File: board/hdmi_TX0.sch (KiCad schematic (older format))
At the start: 21 parts

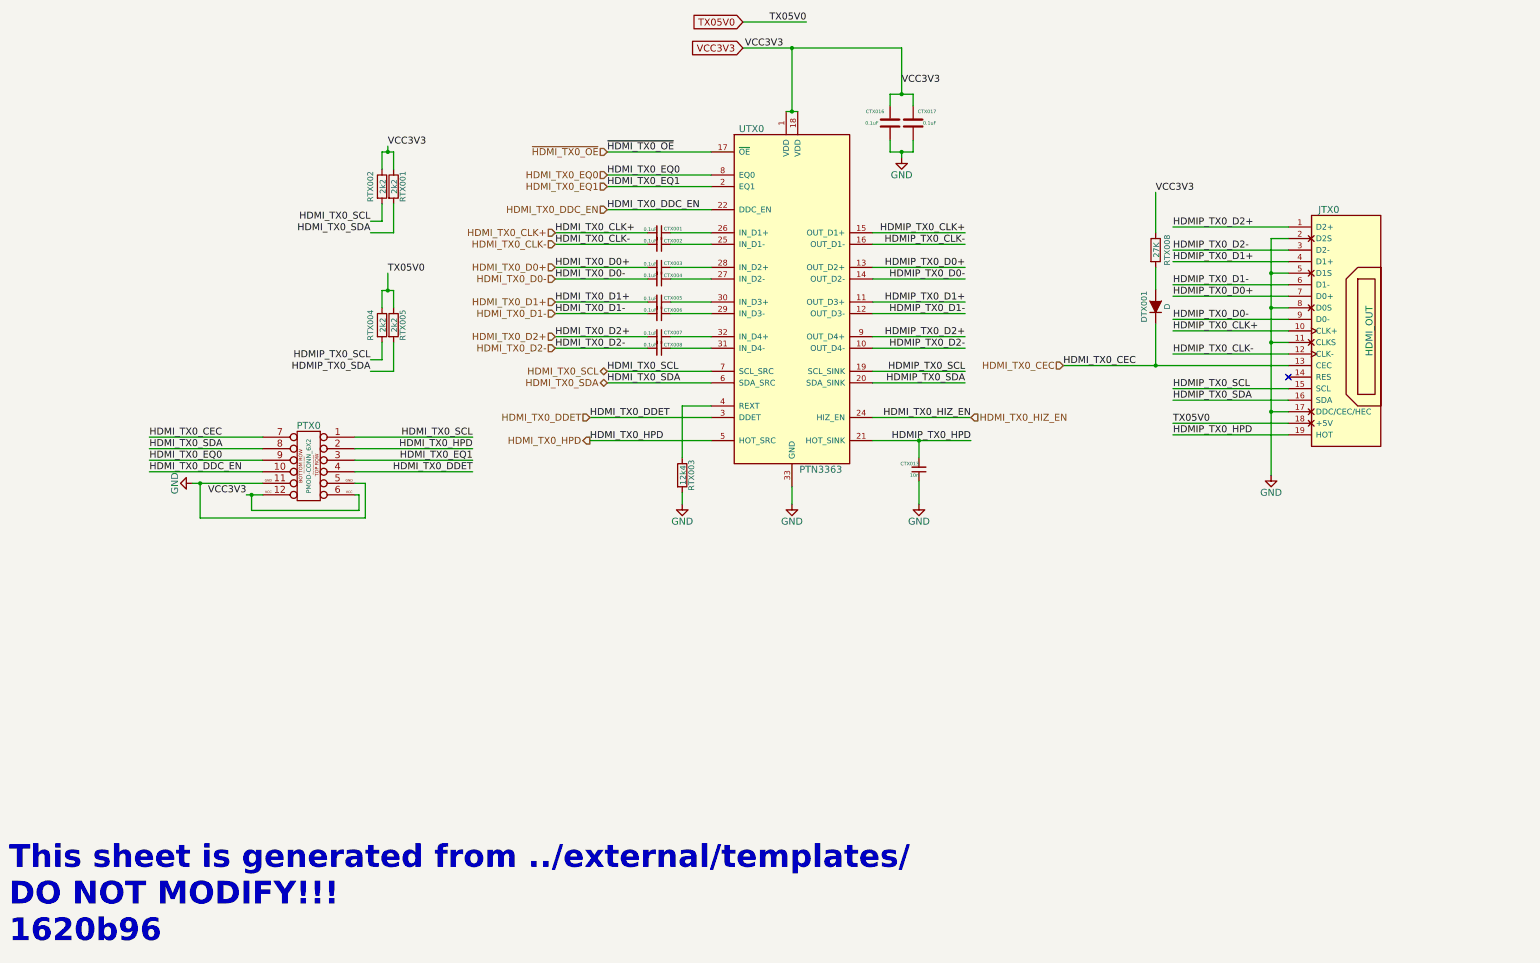
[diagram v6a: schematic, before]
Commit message: Update from template.
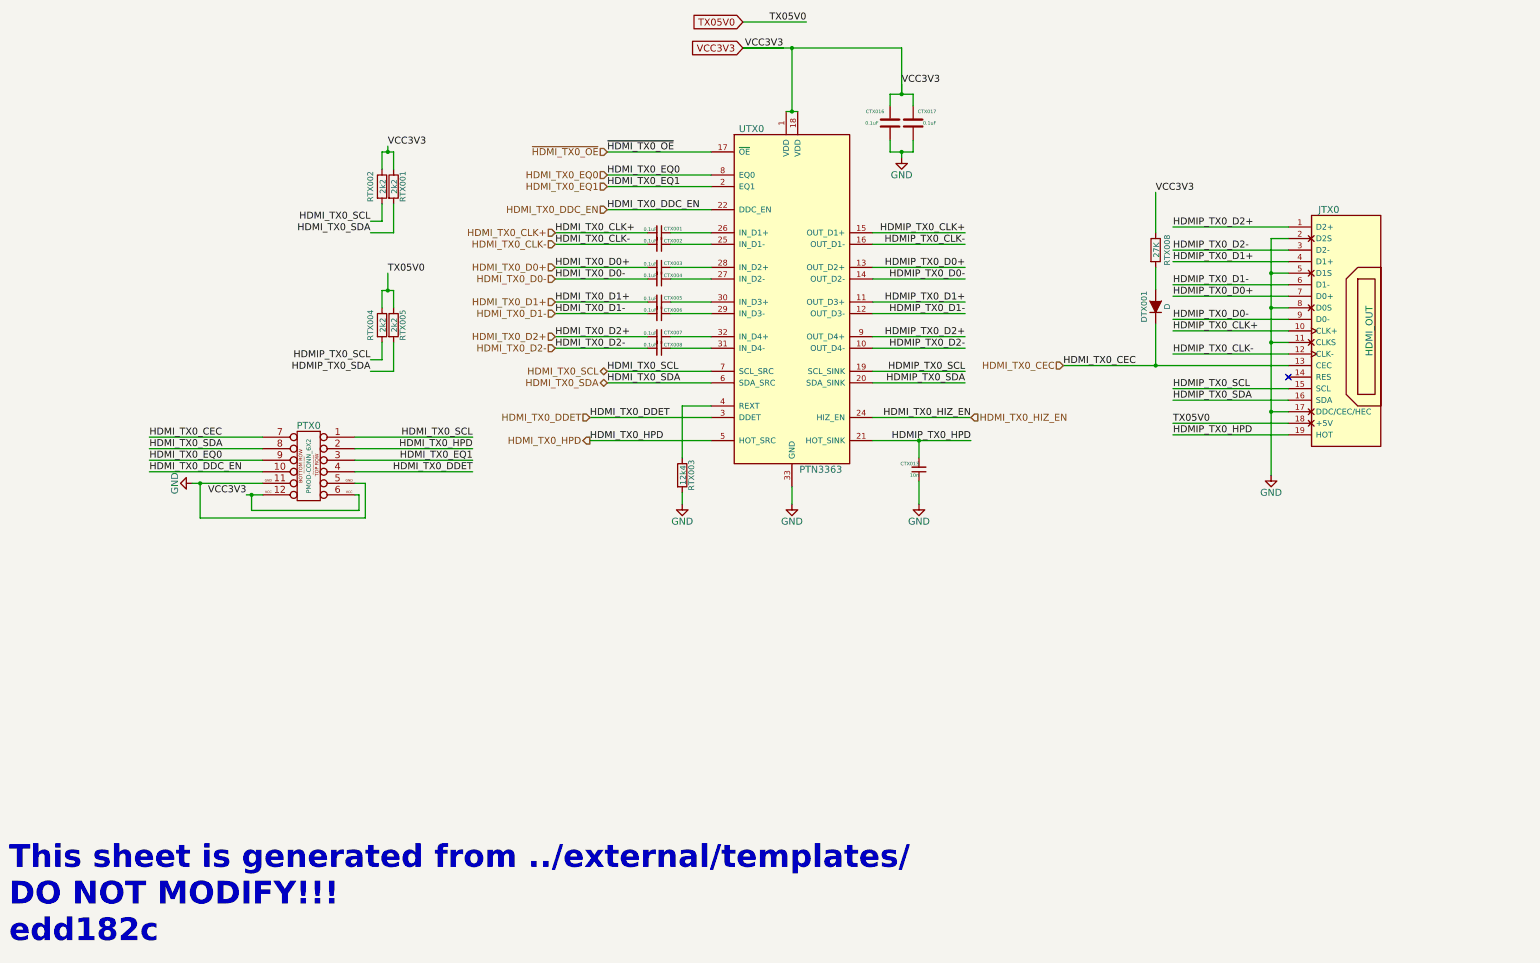
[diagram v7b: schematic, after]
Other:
- note added: "This sheet is generated from ../external/templates/\nDO NOT MODIFY!!!\nedd182c"
- note removed: "This sheet is generated from ../external/templates/\nDO NOT MODIFY!!!\n1620b96"
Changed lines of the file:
@@
 LIBS:contrib
 LIBS:valves
-LIBS:pmod
+LIBS:pmod-conn_6x2
+LIBS:ma78l00
 LIBS:hdmi
 LIBS:ptn3363
-LIBS:ma78l00
-LIBS:pmod-conn_6x2
-LIBS:EEPROM
-LIBS:xc9140
-LIBS:reg710-dbv
-LIBS:pmod-hdmi-tx-cache
 EELAYER 25 0
 EELAYER END
 $Descr A3 16535 11693
 encoding utf-8
-Sheet 2 2
+Sheet 1 1
 Title ""
 Date ""
@@
 HDMIP_TX0_HPD
 $Comp
-L GND #PWR010
+L GND #PWR106
 U 1 1 57B7C214
 P 7450 7150
-F 0 "#PWR010" H 7450 6900 60  0001 C CNN
+F 0 "#PWR106" H 7450 6900 60  0001 C CNN
 F 1 "GND" H 7450 7000 60  0000 C CNN
 F 2 "" H 7450 7150 60  0000 C CNN
@@
 $EndComp
 $Comp
-L GND #PWR011
+L GND #PWR112
 U 1 1 57C0774B
 P 11600 6900
-F 0 "#PWR011" H 11600 6650 60  0001 C CNN
+F 0 "#PWR112" H 11600 6650 60  0001 C CNN
 F 1 "GND" H 11600 6750 60  0000 C CNN
 F 2 "" H 11600 6900 60  0000 C CNN
@@
 AR Path="/57C07751" Ref="RTX008"  Part="1"
 AR Path="/57C01383/57C07751" Ref="RTX003"  Part="1"
-AR Path="/5802F547/57C07751" Ref="RTX008"  Part="1"
 F 0 "RTX008" V 10700 4950 50  0000 C CNN
 F 1 "27K" V 10607 4951 50  0000 C CNN
@@
 AR Path="/57C07753" Ref="RTX002"  Part="1"
 AR Path="/57C01383/57C07753" Ref="RTX001"  Part="1"
-AR Path="/5802F547/57C07753" Ref="RTX002"  Part="1"
 F 0 "RTX002" V 3800 4400 50  0000 C CNN
 F 1 "2k2" V 3907 4401 50  0000 C CNN
@@
 AR Path="/57C07755" Ref="RTX001"  Part="1"
 AR Path="/57C01383/57C07755" Ref="RTX002"  Part="1"
-AR Path="/5802F547/57C07755" Ref="RTX001"  Part="1"
 F 0 "RTX001" V 4080 4400 50  0000 C CNN
 F 1 "2k2" V 4007 4401 50  0000 C CNN
@@
 	11750 4850 11600 4850
 Wire Wire Line
-	11600 4850 11600 6900
+	11600 4850 11600 5150
+Wire Wire Line
+	11600 5150 11600 5450
+Wire Wire Line
+	11600 5450 11600 5750
+Wire Wire Line
+	11600 5750 11600 6350
+Wire Wire Line
+	11600 6350 11600 6900
 Wire Wire Line
 	11750 5150 11600 5150
@@
 	6400 5800 6750 5800
 Wire Wire Line
-	8150 6600 9000 6600
+	8150 6600 8550 6600
+Wire Wire Line
+	8550 6600 9000 6600
 Wire Wire Line
 	8150 6400 9000 6400
 Wire Wire Line
-	7400 3750 7500 3750
-Wire Wire Line
-	7450 3200 7450 3750
+	7400 3750 7450 3750
+Wire Wire Line
+	7450 3750 7500 3750
+Wire Wire Line
+	7450 3750 7450 3200
 Connection ~ 7450 3750
 Wire Wire Line
@@
 Connection ~ 11600 6350
 Wire Wire Line
-	9800 5950 11750 5950
+	9800 5950 10600 5950
+Wire Wire Line
+	10600 5950 11750 5950
 Wire Wire Line
 	10600 5950 10600 5590
@@
 	4000 4100 4000 4250
 Wire Wire Line
-	3900 4100 4000 4100
+	3900 4100 3950 4100
+Wire Wire Line
+	3950 4100 4000 4100
 Text Label 3800 5900 2    60   ~ 0
 HDMIP_TX0_SCL
@@
 AR Path="/57C07769" Ref="RTX004"  Part="1"
 AR Path="/57C01383/57C07769" Ref="RTX004"  Part="1"
-AR Path="/5802F547/57C07769" Ref="RTX004"  Part="1"
 F 0 "RTX004" V 3800 5600 50  0000 C CNN
 F 1 "2k2" V 3907 5601 50  0000 C CNN
@@
 AR Path="/57B7FCE7" Ref="RTX005"  Part="1"
 AR Path="/57C01383/57B7FCE7" Ref="RTX005"  Part="1"
-AR Path="/5802F547/57B7FCE7" Ref="RTX005"  Part="1"
 F 0 "RTX005" V 4080 5600 50  0000 C CNN
 F 1 "2k2" V 4007 5601 50  0000 C CNN
@@
 AR Path="/57C0776D" Ref="RTX003"  Part="1"
 AR Path="/57C01383/57C0776D" Ref="RTX006"  Part="1"
-AR Path="/5802F547/57C0776D" Ref="RTX003"  Part="1"
 F 0 "RTX003" V 6580 6900 50  0000 C CNN
 F 1 "12k4" V 6507 6901 50  0000 C CNN
@@
 	6500 6300 6500 6750
 $Comp
-L GND #PWR012
+L GND #PWR104
 U 1 1 57C0776F
 P 6500 7150
-F 0 "#PWR012" H 6500 6900 60  0001 C CNN
+F 0 "#PWR104" H 6500 6900 60  0001 C CNN
 F 1 "GND" H 6500 7000 60  0000 C CNN
 F 2 "" H 6500 7150 60  0000 C CNN
@@
 	3900 5300 3900 5450
 Wire Wire Line
-	3900 5300 4000 5300
+	3900 5300 3950 5300
+Wire Wire Line
+	3950 5300 4000 5300
 Wire Wire Line
 	4000 5300 4000 5450
@@
 $EndComp
 $Comp
-L GND #PWR013
+L GND #PWR109
 U 1 1 57C07776
 P 8550 7150
-F 0 "#PWR013" H 8550 6900 60  0001 C CNN
+F 0 "#PWR109" H 8550 6900 60  0001 C CNN
 F 1 "GND" H 8550 7000 60  0000 C CNN
 F 2 "" H 8550 7150 60  0000 C CNN
@@
 AR Path="/57C07777" Ref="CTX017"  Part="1"
 AR Path="/57C01383/57C07777" Ref="CTX002"  Part="1"
-AR Path="/5802F547/57C07777" Ref="CTX017"  Part="1"
 F 0 "CTX017" H 8300 3750 30  0000 L CNN
 F 1 "0.1uF" H 8300 3850 30  0000 L CNN
@@
 AR Path="/57C07779" Ref="CTX016"  Part="1"
 AR Path="/57C01383/57C07779" Ref="CTX001"  Part="1"
-AR Path="/5802F547/57C07779" Ref="CTX016"  Part="1"
 F 0 "CTX016" H 8350 3750 30  0000 L CNN
 F 1 "0.1uF" H 8400 3850 30  0000 L CNN
@@
 $EndComp
 Wire Wire Line
-	8300 3600 8500 3600
+	8300 3600 8400 3600
+Wire Wire Line
+	8400 3600 8500 3600
 Wire Wire Line
 	8300 3600 8300 3700
@@
 	8300 4000 8300 4100
 Wire Wire Line
-	8300 4100 8500 4100
+	8300 4100 8400 4100
+Wire Wire Line
+	8400 4100 8500 4100
 Wire Wire Line
 	8500 4100 8500 4000
 $Comp
-L GND #PWR014
+L GND #PWR108
 U 1 1 57C0777E
 P 8400 4150
-F 0 "#PWR014" H 8400 3900 60  0001 C CNN
+F 0 "#PWR108" H 8400 3900 60  0001 C CNN
 F 1 "GND" H 8400 4000 60  0000 C CNN
 F 2 "" H 8400 4150 60  0000 C CNN
@@
 HDMI_TX0_SDA
 $Comp
-L GND #PWR015
+L GND #PWR101
 U 1 1 57C07784
 P 2255 6970
-F 0 "#PWR015" H 2255 6720 60  0001 C CNN
+F 0 "#PWR101" H 2255 6720 60  0001 C CNN
 F 1 "GND" H 2255 6820 60  0000 C CNN
 F 2 "" H 2255 6970 60  0000 C CNN
@@
 	6500 7050 6500 7150
 Text Notes 670  10960 0    197  ~ 39
-This sheet is generated from ../external/templates/\nDO NOT MODIFY!!!\n1620b96
-Wire Wire Line
-	2255 6970 2865 6970
-Wire Wire Line
-	2725 7070 2865 7070
+This sheet is generated from ../external/templates/\nDO NOT MODIFY!!!\nedd182c
+Wire Wire Line
+	2255 6970 2325 6970
+Wire Wire Line
+	2325 6970 2865 6970
+Wire Wire Line
+	2725 7070 2770 7070
+Wire Wire Line
+	2770 7070 2865 7070
 Wire Wire Line
 	2865 6570 1885 6570
@@
 VCC3V3
 Wire Wire Line
-	7025 3200 8400 3200
+	7025 3200 7375 3200
 $Comp
 L PMOD-CONN_6X2 PTX0
@@
 $EndComp
 Wire Wire Line
-	8400 3200 8400 3600
+	8400 3600 8400 3515
 Text Label 8400 3515 0    60   ~ 0
 VCC3V3
@@
 Text GLabel 7025 2975 0    60   Input ~ 0
 TX05V0
+Wire Wire Line
+	7025 3200 7450 3200
+Wire Wire Line
+	7450 3200 8400 3200
+Wire Wire Line
+	8400 3200 8400 3600
 Connection ~ 7450 3200
 Wire Wire Line

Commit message: Update from templates + s/HPD/HOT/ + s/HPA/HOT/
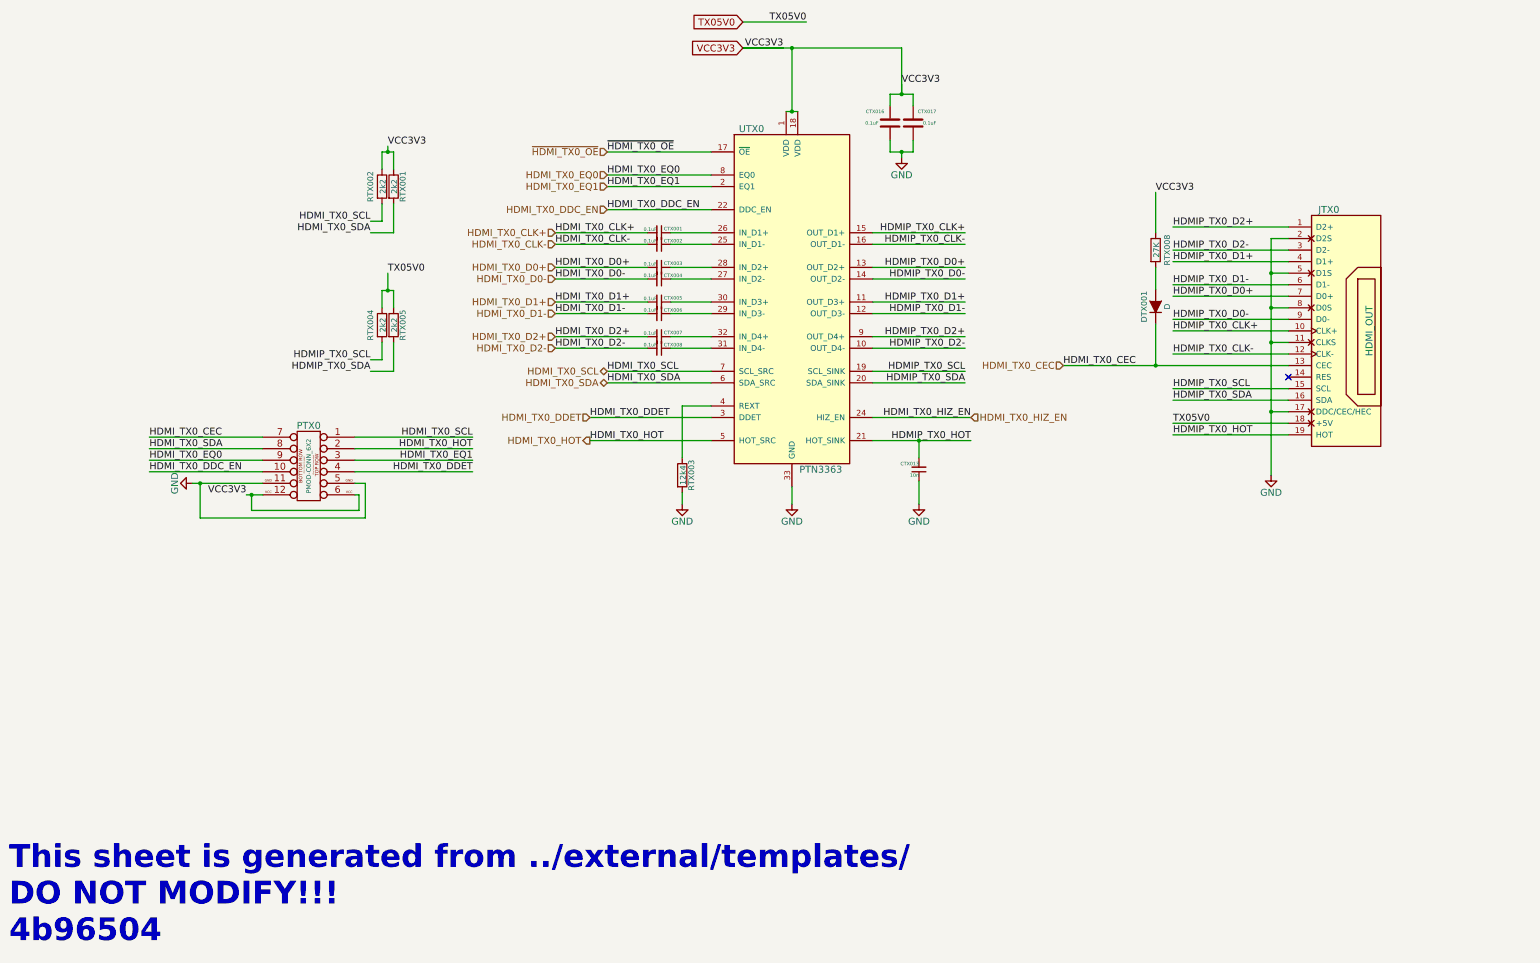
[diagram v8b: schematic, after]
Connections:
- net HDMIP_TX0_HPD renamed HDMIP_TX0_HOT
- net HDMI_TX0_HPD renamed HDMI_TX0_HOT
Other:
- note added: "This sheet is generated from ../external/templates/\nDO NOT MODIFY!!!\n4b96504"
- note removed: "This sheet is generated from ../external/templates/\nDO NOT MODIFY!!!\nedd182c"
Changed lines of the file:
@@
 TX05V0
 Text Label 9000 6600 2    60   ~ 0
-HDMIP_TX0_HPD
+HDMIP_TX0_HOT
 Text Label 10750 6550 0    60   ~ 0
-HDMIP_TX0_HPD
+HDMIP_TX0_HOT
 $Comp
 L GND #PWR106
@@
 	6500 7150 6500 7150
 Text Label 5700 6600 0    60   ~ 0
-HDMI_TX0_HPD
+HDMI_TX0_HOT
 Text Label 3800 4700 2    60   ~ 0
 HDMI_TX0_SCL
@@
 HDMI_TX0_HIZ_EN
 Text Label 4685 6670 2    60   ~ 0
-HDMI_TX0_HPD
+HDMI_TX0_HOT
 Text Label 4685 6570 2    60   ~ 0
 HDMI_TX0_SCL
@@
 HDMI_TX0_DDET
 Text HLabel 5700 6600 0    60   Output ~ 0
-HDMI_TX0_HPD
+HDMI_TX0_HOT
 Text HLabel 9000 6400 2    60   Input ~ 0
 HDMI_TX0_HIZ_EN
@@
 	6500 7050 6500 7150
 Text Notes 670  10960 0    197  ~ 39
-This sheet is generated from ../external/templates/\nDO NOT MODIFY!!!\nedd182c
+This sheet is generated from ../external/templates/\nDO NOT MODIFY!!!\n4b96504
 Wire Wire Line
 	2255 6970 2325 6970
